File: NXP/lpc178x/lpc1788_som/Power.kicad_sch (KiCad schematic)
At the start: 7 parts, among them J2 USB_C_Receptacle_USB2.0_16P, Q1 DMG2302U, U4 AP7361C-33E

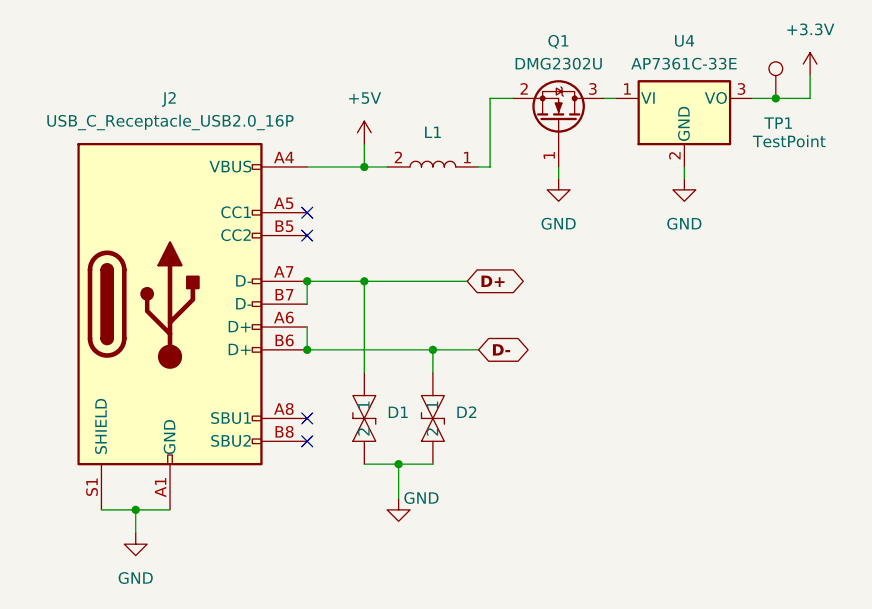
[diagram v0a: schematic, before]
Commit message: LPC1788
Added LPC1788 som module
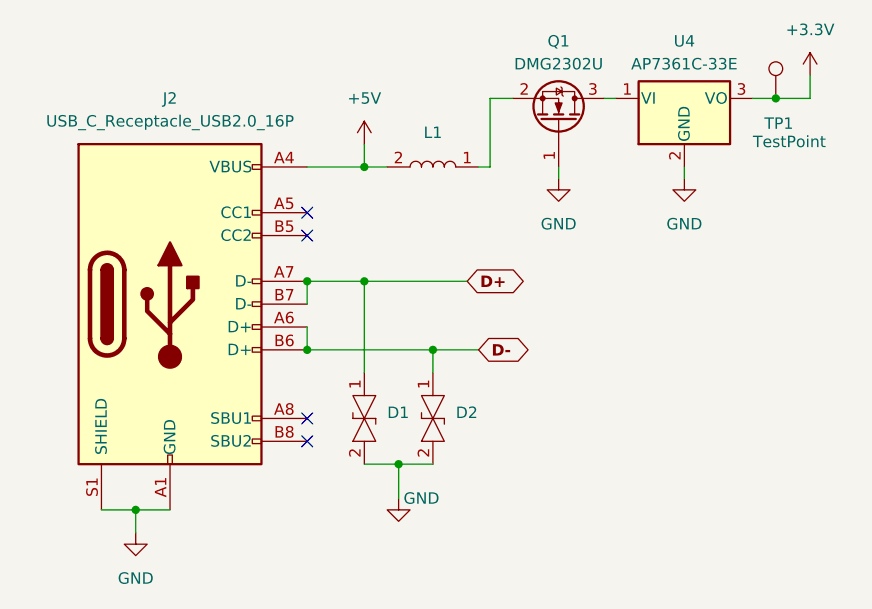
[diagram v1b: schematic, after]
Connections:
- net D+: now also D1.1; no longer D1. (2)
- net D-: now also D2.1; no longer D2. (2)
- net GND: now also D1.2, D2.2; no longer D1. (2), D2. (2)
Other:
- moved on the sheet: D1, D2
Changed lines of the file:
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@@
 		)
 		(property "Footprint" "Local_Footprints:smd_pad_1.27m_0.76m"
-			(at 138.43 110.49 0)
+			(at 134.62 110.49 0)
 			(effects
 				(font
@@
 			)
 		)
-		(pin ""
-		)
-		(pin ""
+		(pin "2"
+		)
+		(pin "1"
 		)
 		(instances
@@
 	)
 	(symbol
+		(lib_name "PGB1010603NR_1")
 		(lib_id "Local_symbols:PGB1010603NR")
 		(at 146.05 110.49 90)
@@
 		)
 		(property "Footprint" "Local_Footprints:smd_pad_1.27m_0.76m"
-			(at 146.05 110.49 0)
+			(at 142.494 110.49 0)
 			(effects
 				(font
@@
 			)
 		)
-		(pin ""
-		)
-		(pin ""
-		)
-		(instances
+		(pin "2"
+		)
+		(pin "1"
+		)
+		(instances
